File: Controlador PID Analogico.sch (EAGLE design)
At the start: 7 parts, among them IC1 LF353N, IC2 LF353N, IC3 LF353N, IC4 X9C102P

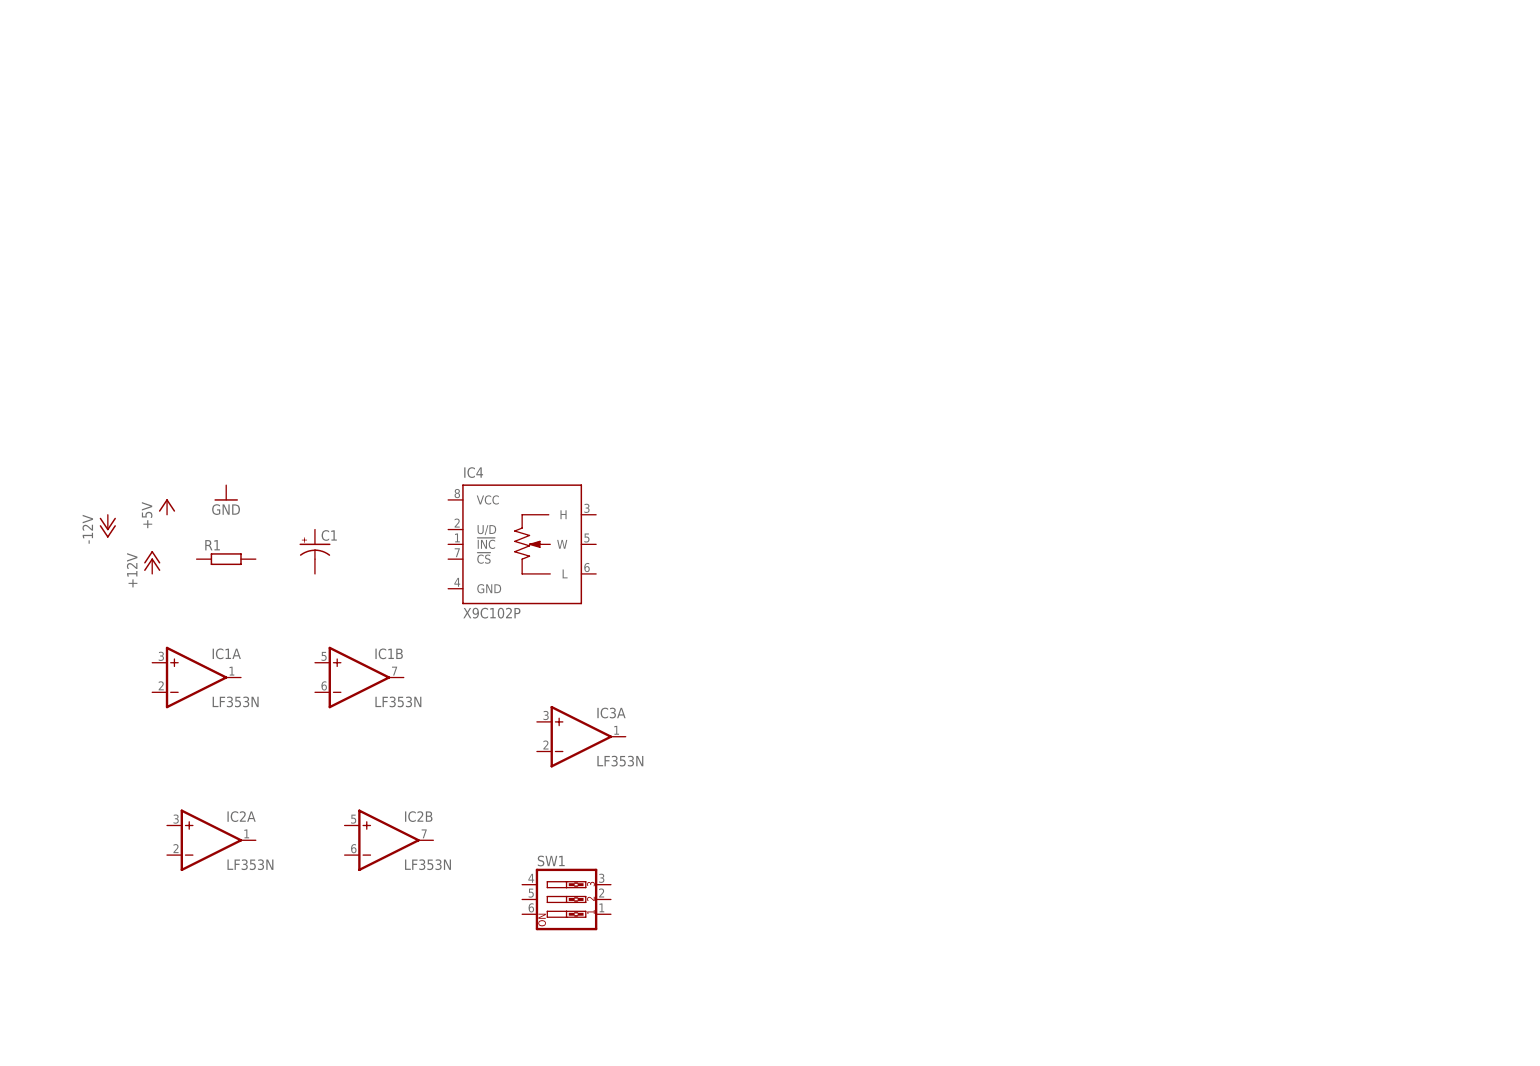
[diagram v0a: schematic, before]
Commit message: Terminado etapa restador y las tres acciones de control
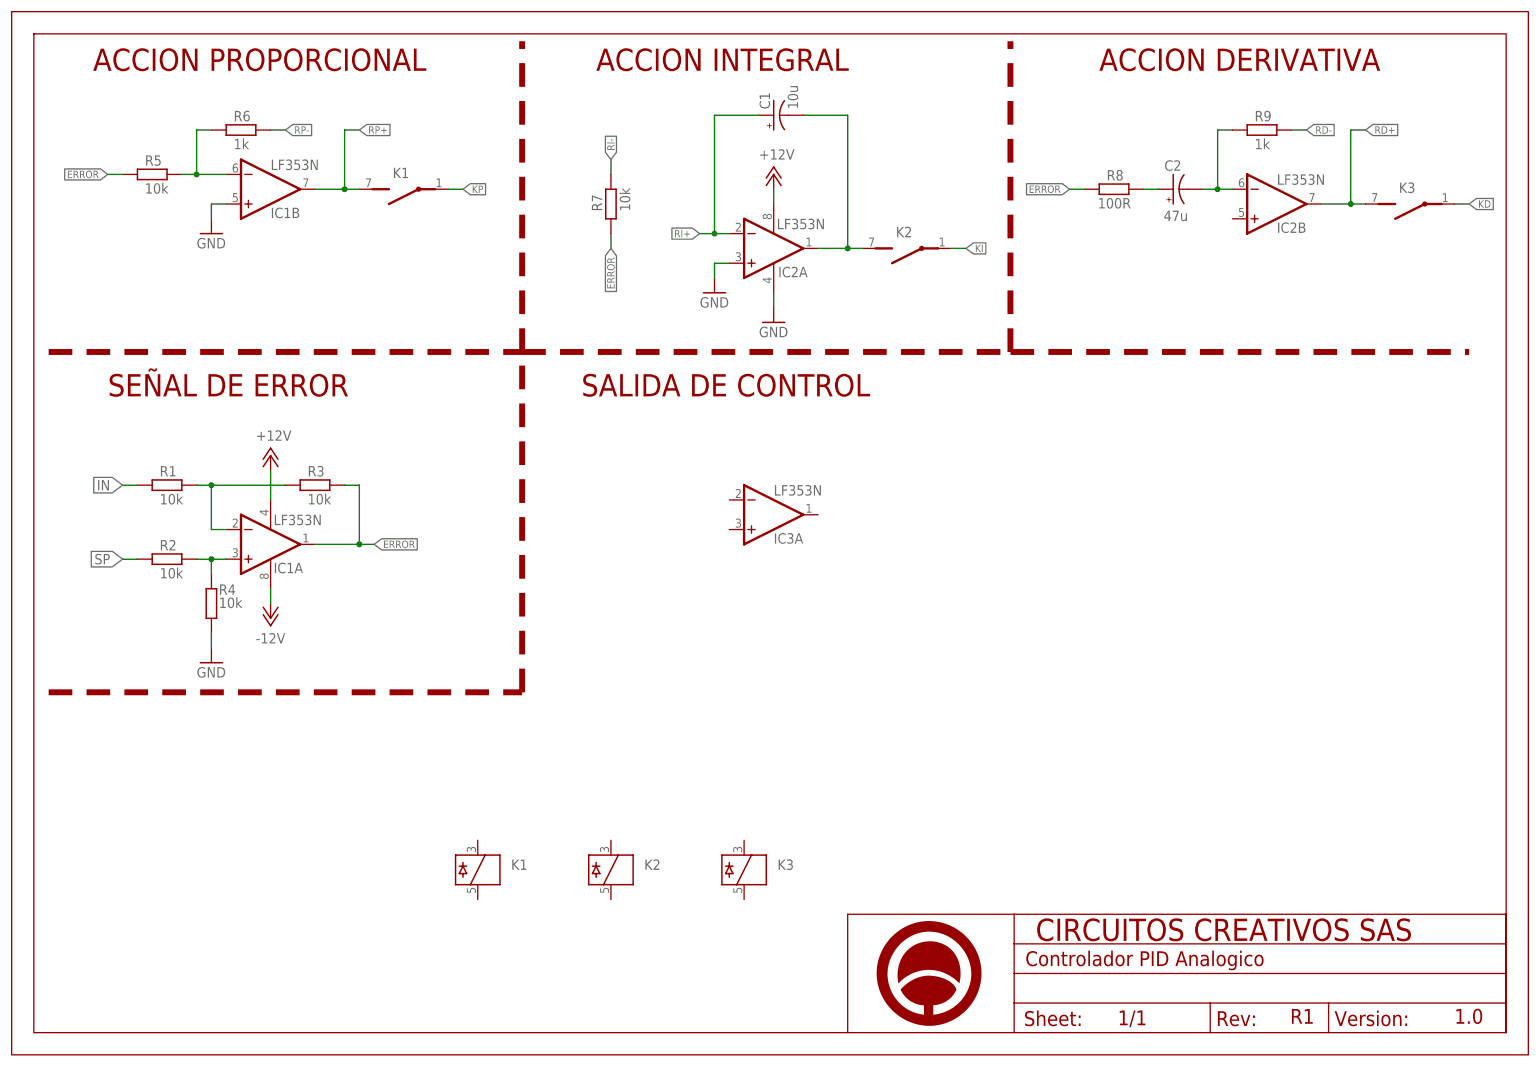
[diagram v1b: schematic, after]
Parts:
- removed IC4: X9C102P, pot-xicor:X9C102P
- removed SW1: (no value), special:SW_DIP-3
- added C2: 47u, rcl:CPOL-USE2,5-6E
- added K1, K2, K3: 35701331, relay:35701331
- added R2, R3, R4, R5, R7: 10k, rcl:R-EU_0204/7
- added R6, R9: 1k, rcl:R-EU_0204/7
- added R8: 100R, rcl:R-EU_0204/7
- added U$1: A4_HORIZONTAL, Circuitos-Creativos-Estilos:A4_HORIZONTAL
- C1: value (none) -> 10u
- R1: value (none) -> 10k
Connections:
- new net +12V: IC1P.V-, IC2P.V+
- new net -12V: IC1P.V+
- new net ERROR: IC1A.OUT, R3.2, R5.2, R7.2, R8.1
- new net GND: IC1B.+IN, IC2A.+IN, IC2P.V-, R4.2
- new net IN: R1.1
- new net KD: K32.P
- new net KI: K22.P
- new net KP: K12.P
- new net N$1: IC1A.-IN, R1.2, R3.1
- new net N$2: IC1A.+IN, R2.2, R4.1
- new net N$3: IC1B.-IN, R5.1, R6.1
- new net N$4: C1.-, IC2A.OUT, K22.S
- new net N$5: C2.-, IC2B.-IN, R9.1
- new net N$6: C2.+, R8.2
- new net RD+: IC2B.OUT, K32.S
- new net RD-: R9.2
- new net RI+: C1.+, IC2A.-IN
- new net RI-: R7.1
- new net RP+: IC1B.OUT, K12.S
- new net RP-: R6.2
- new net SP: R2.1
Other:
- note added: "1.0"
- note added: "ACCION DERIVATIVA"
- note added: "ACCION INTEGRAL"
- note added: "ACCION PROPORCIONAL"
- note added: "R1"
- note added: "SALIDA DE CONTROL"
- note added: "SEÑAL DE ERROR"
- moved on the sheet: C1, IC1A, IC1B, IC2A, IC2B, IC3A, R1

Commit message: Terminado SCH y BRD. generando los Gerber
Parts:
- added PWR, PWR1: (no value), con-ptr500:AK500/2
- added Q1, Q2, Q3: 2N3904, transistor-small-signal:2N3904
- added R10, R11, R12, R13: 47k, rcl:R-EU_0204/7
- added R14, R15, R16: 10k, rcl:R-EU_0204/7
- added X1: 2520-5, con-3m:2520-5
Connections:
- new net +5V: K11.3, K21.3, K31.3, PWR-1.KL, PWR1-1.KL
- new net N$10: Q2.B, R15.2
- new net N$11: K21.5, Q2.C
- new net N$12: Q3.B, R16.2
- new net N$13: K31.5, Q3.C
- new net N$7: IC3A.-IN, R10.2, R11.2, R12.2, R13.1
- new net N$8: Q1.B, R14.2
- new net N$9: K11.5, Q1.C
- new net OUT: IC3A.OUT, R13.2
- new net VD: K32.P, R12.1
- new net VI: K22.P, R10.1
- new net VP: K12.P, R11.1
- net +12V: now also IC1P.V+, IC3P.V+; no longer IC1P.V-
- net -12V: now also IC1P.V-, IC2P.V-, IC3P.V-; no longer IC1P.V+
- net GND: now also IC2B.+IN, IC3A.+IN, PWR-2.KL, PWR1-2.KL, Q1.E, Q2.E, Q3.E; no longer IC2P.V-
- net KD: now also R16.1, X1-1.KL; no longer K32.P
- net KI: now also R15.1, X1-3.KL; no longer K22.P
- net KP: now also R14.1, X1-5.KL; no longer K12.P
- net RD+: now also X1-9.KL
- net RD-: now also X1-7.KL
- net RI+: now also X1-17.KL
- net RI-: now also X1-18.KL
- net RP+: now also X1-19.KL
- net RP-: now also X1-20.KL
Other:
- note added: "ACTIVACION RELES"
- note added: "CONECTOR POT DIGITALES"
- moved on the sheet: IC1A, IC3A, K1, K2, K3, R1, R2, R3, R4
